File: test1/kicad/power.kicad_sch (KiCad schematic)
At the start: 14 parts, among them J1 1x2 100mil, J2 1x2 100mil, J3 1x2 100mil, U1 TPS7A8401A, U2 TPS22916

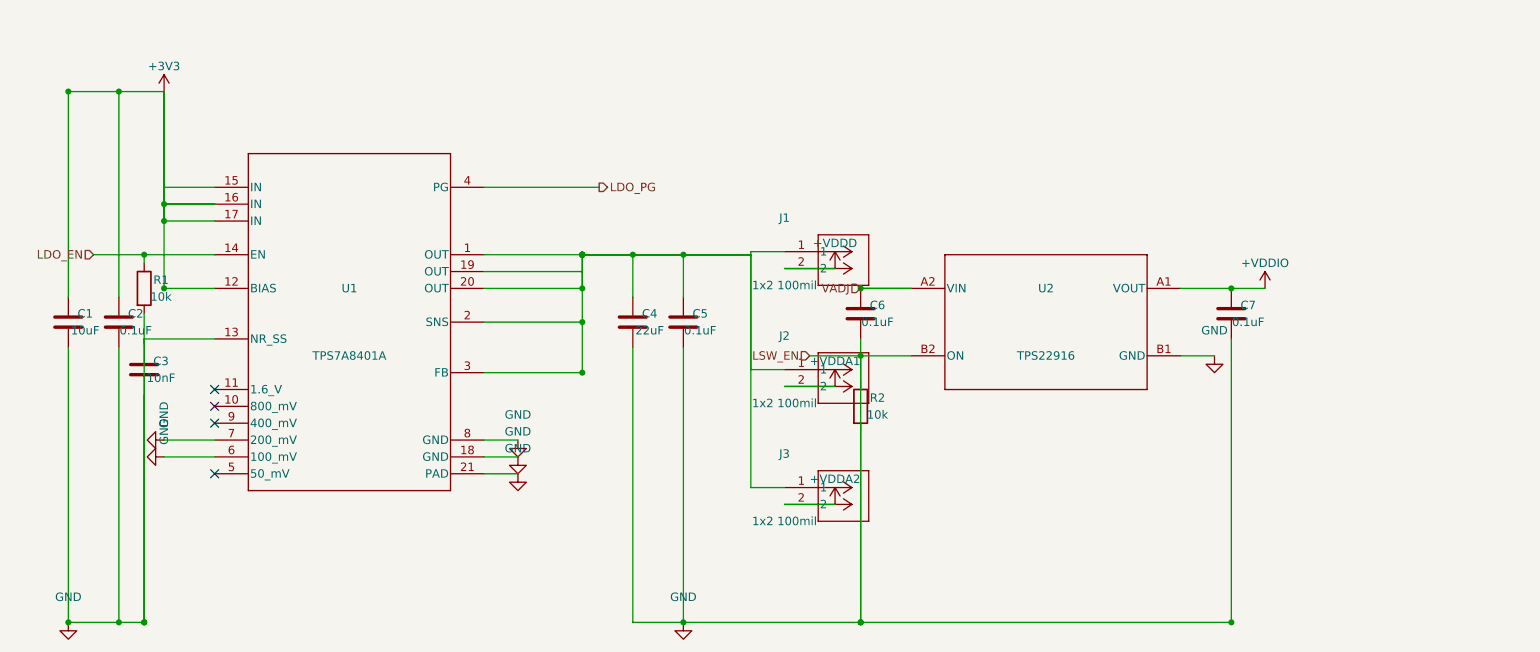
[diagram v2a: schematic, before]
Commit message: Power: separate load-switch cluster from jumper column
The TPS22916 cluster (VADJ label, C6, R2, U2, C7, +VDDIO) was sitting
~4 mm from the jumper column's +VDDx power-symbol labels. R2 and the
LSW_EN hier label collided visually with J2's body.

Fixes:
  - Moved U2 from x=235 → x=270 (35 mm right of jumper power symbols).
  - Reanchored C6, R2, VADJ, and LSW_EN positions to U2 pin coords (no
    hardcoded x), so the whole cluster moves as one if U2 is repositioned
    again.
  - Cleaned up redundant short wire (C6 top → VIN already covered by the
    VADJ→VIN horizontal that passes through C6's pin).

Skill update: cluster separation rule now mentions the label-bounding-box
distance, not just body-to-body — default to ≥25 mm when both adjacent
clusters have side-pointing power symbols or hier labels.

Memory: appended two more lessons to feedback_kicad_generator_lessons.md
(cluster-separation, and "anchor cluster coords to chip pin coords, not
hardcoded constants").

Co-Authored-By: Claude Opus 4.7 (1M context) <noreply@anthropic.com>
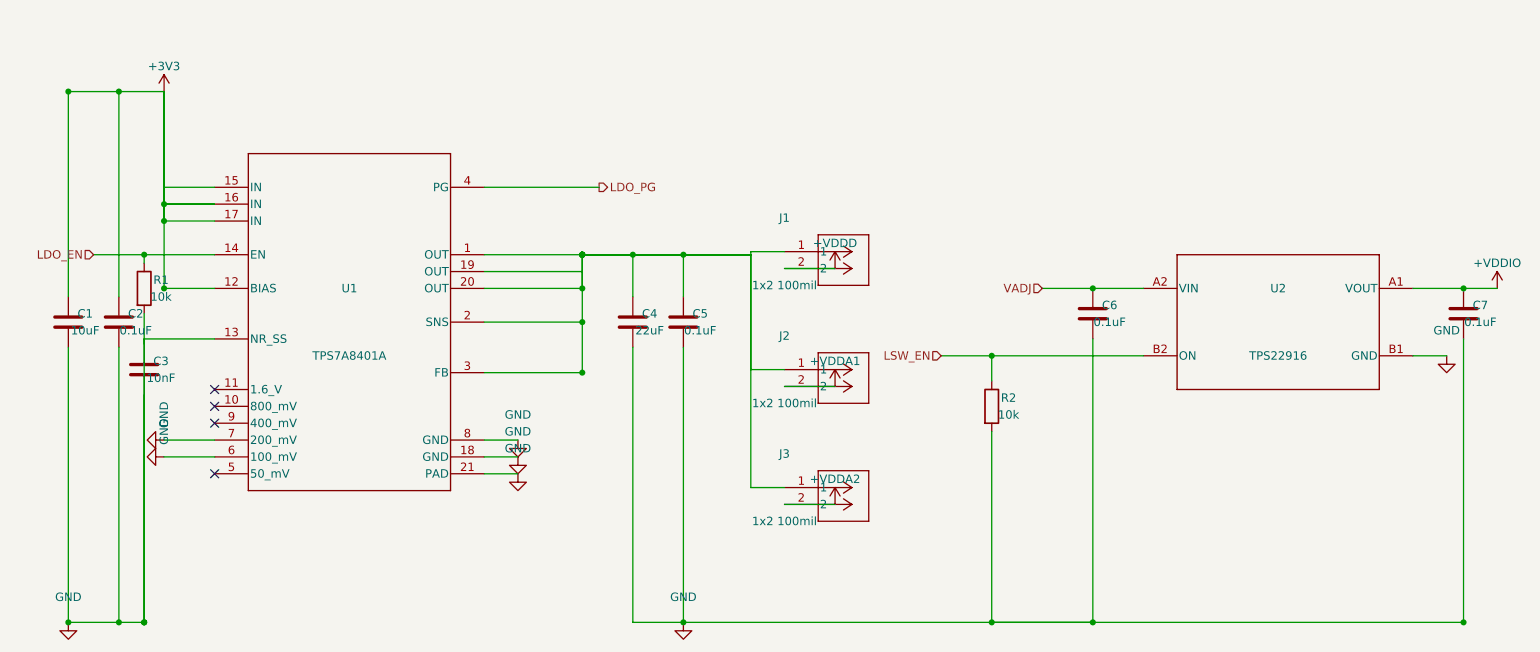
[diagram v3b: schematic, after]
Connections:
- net GND: no longer R2.1, U2.B2 (ON)
- new net LSW_EN: R2.1, U2.B2 (ON)
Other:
- moved on the sheet: C6, C7, R2, U2
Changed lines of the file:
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@@
   (symbol
     (lib_id "Lib:TPS22916CNYFPR")
-    (at 235 130 0)
+    (at 270 130 0)
     (unit 1) (in_bom yes) (on_board yes) (dnp no)
-    (property "Reference" "U2" (at 235 124.92 0) (effects (font (size 1.27 1.27))))
-    (property "Value" "TPS22916" (at 235 135.08 0) (effects (font (size 1.27 1.27))))
+    (property "Reference" "U2" (at 270 124.92 0) (effects (font (size 1.27 1.27))))
+    (property "Value" "TPS22916" (at 270 135.08 0) (effects (font (size 1.27 1.27))))
     (property "Footprint" "Package_DirectFETandLGA:Texas_DSBGA-4_0.6x1.0mm_Layout2x2_P0.4mm" (at 0 0 0) (effects (font (size 1.27 1.27)) (hide yes)))
     (property "Datasheet" "" (at 0 0 0) (effects (font (size 1.27 1.27)) (hide yes)))
@@
       (project "test1"
         (path "/4ed7a046-ef33-57d9-8730-321c05965af3/45af8917-b3aa-56de-8c9b-8d649d910e5f" (reference "U2") (unit 1)))))
-  (wire (pts (xy 214.68 124.92) (xy 207.01 124.92)) (stroke (width 0) (type default)))
-  (hierarchical_label "VADJ" (shape input) (at 207.01 124.92 180) (effects (font (size 1.27 1.27)) (justify right)))
-  (wire (pts (xy 255.32 135.08) (xy 260.4 135.08)) (stroke (width 0) (type default)))
+  (wire (pts (xy 249.68 124.92) (xy 234.44 124.92)) (stroke (width 0) (type default)))
+  (hierarchical_label "VADJ" (shape input) (at 234.44 124.92 180) (effects (font (size 1.27 1.27)) (justify right)))
+  (wire (pts (xy 290.32 135.08) (xy 295.4 135.08)) (stroke (width 0) (type default)))
   (symbol
     (lib_id "power:GND")
-    (at 260.4 135.08 0)
+    (at 295.4 135.08 0)
     (unit 1) (in_bom yes) (on_board yes) (dnp no)
-    (property "Reference" "#PWR151762a4" (at 260.4 128.73000000000002 0) (effects (font (size 1.27 1.27)) (hide yes)))
-    (property "Value" "GND" (at 260.4 131.27 0) (effects (font (size 1.27 1.27))))
+    (property "Reference" "#PWRf65ce50a" (at 295.4 128.73000000000002 0) (effects (font (size 1.27 1.27)) (hide yes)))
+    (property "Value" "GND" (at 295.4 131.27 0) (effects (font (size 1.27 1.27))))
     (property "Footprint" "" (at 0 0 0) (effects (font (size 1.27 1.27)) (hide yes)))
     (property "Datasheet" "" (at 0 0 0) (effects (font (size 1.27 1.27)) (hide yes)))
@@
     (instances
       (project "test1"
-        (path "/4ed7a046-ef33-57d9-8730-321c05965af3/45af8917-b3aa-56de-8c9b-8d649d910e5f" (reference "#PWR151762a4") (unit 1)))))
-  (wire (pts (xy 255.32 124.92) (xy 268.02 124.92)) (stroke (width 0) (type default)))
+        (path "/4ed7a046-ef33-57d9-8730-321c05965af3/45af8917-b3aa-56de-8c9b-8d649d910e5f" (reference "#PWRf65ce50a") (unit 1)))))
+  (wire (pts (xy 290.32 124.92) (xy 303.02 124.92)) (stroke (width 0) (type default)))
   (symbol
     (lib_id "power:+VDDIO")
-    (at 268.02 124.92 0)
+    (at 303.02 124.92 0)
     (unit 1) (in_bom yes) (on_board yes) (dnp no)
-    (property "Reference" "#PWR666eeb67" (at 268.02 118.57000000000001 0) (effects (font (size 1.27 1.27)) (hide yes)))
-    (property "Value" "+VDDIO" (at 268.02 121.11 0) (effects (font (size 1.27 1.27))))
+    (property "Reference" "#PWRd893e26a" (at 303.02 118.57000000000001 0) (effects (font (size 1.27 1.27)) (hide yes)))
+    (property "Value" "+VDDIO" (at 303.02 121.11 0) (effects (font (size 1.27 1.27))))
     (property "Footprint" "" (at 0 0 0) (effects (font (size 1.27 1.27)) (hide yes)))
     (property "Datasheet" "" (at 0 0 0) (effects (font (size 1.27 1.27)) (hide yes)))
@@
     (instances
       (project "test1"
-        (path "/4ed7a046-ef33-57d9-8730-321c05965af3/45af8917-b3aa-56de-8c9b-8d649d910e5f" (reference "#PWR666eeb67") (unit 1)))))
+        (path "/4ed7a046-ef33-57d9-8730-321c05965af3/45af8917-b3aa-56de-8c9b-8d649d910e5f" (reference "#PWRd893e26a") (unit 1)))))
   (symbol
     (lib_id "Device:C")
-    (at 207.06 128.73 0)
+    (at 242.06 128.73 0)
     (unit 1) (in_bom yes) (on_board yes) (dnp no)
-    (property "Reference" "C6" (at 209.6 127.46 0) (effects (font (size 1.27 1.27))))
-    (property "Value" "0.1uF" (at 209.6 130.0 0) (effects (font (size 1.27 1.27))))
+    (property "Reference" "C6" (at 244.6 127.46 0) (effects (font (size 1.27 1.27))))
+    (property "Value" "0.1uF" (at 244.6 130.0 0) (effects (font (size 1.27 1.27))))
     (property "Footprint" "Capacitor_SMD:C_0402_1005Metric" (at 0 0 0) (effects (font (size 1.27 1.27)) (hide yes)))
     (property "Datasheet" "" (at 0 0 0) (effects (font (size 1.27 1.27)) (hide yes)))
@@
       (project "test1"
         (path "/4ed7a046-ef33-57d9-8730-321c05965af3/45af8917-b3aa-56de-8c9b-8d649d910e5f" (reference "C6") (unit 1)))))
-  (wire (pts (xy 207.06 124.92) (xy 214.68 124.92)) (stroke (width 0) (type default)))
-  (junction (at 207.06 124.92) (diameter 0) (color 0 0 0 0))
-  (wire (pts (xy 207.06 132.54) (xy 207.06 175.26)) (stroke (width 0) (type default)))
-  (wire (pts (xy 207.06 175.26) (xy 180.34 175.26)) (stroke (width 0) (type default)))
-  (junction (at 207.06 175.26) (diameter 0) (color 0 0 0 0))
+  (junction (at 242.06 124.92) (diameter 0) (color 0 0 0 0))
+  (wire (pts (xy 242.06 132.54) (xy 242.06 175.26)) (stroke (width 0) (type default)))
+  (wire (pts (xy 242.06 175.26) (xy 180.34 175.26)) (stroke (width 0) (type default)))
+  (junction (at 242.06 175.26) (diameter 0) (color 0 0 0 0))
   (symbol
     (lib_id "Device:C")
-    (at 262.94 128.73 0)
+    (at 297.94 128.73 0)
     (unit 1) (in_bom yes) (on_board yes) (dnp no)
-    (property "Reference" "C7" (at 265.48 127.46 0) (effects (font (size 1.27 1.27))))
-    (property "Value" "0.1uF" (at 265.48 130.0 0) (effects (font (size 1.27 1.27))))
+    (property "Reference" "C7" (at 300.48 127.46 0) (effects (font (size 1.27 1.27))))
+    (property "Value" "0.1uF" (at 300.48 130.0 0) (effects (font (size 1.27 1.27))))
     (property "Footprint" "Capacitor_SMD:C_0402_1005Metric" (at 0 0 0) (effects (font (size 1.27 1.27)) (hide yes)))
     (property "Datasheet" "" (at 0 0 0) (effects (font (size 1.27 1.27)) (hide yes)))
@@
       (project "test1"
         (path "/4ed7a046-ef33-57d9-8730-321c05965af3/45af8917-b3aa-56de-8c9b-8d649d910e5f" (reference "C7") (unit 1)))))
-  (wire (pts (xy 262.94 124.92) (xy 262.94 124.92)) (stroke (width 0) (type default)))
-  (junction (at 262.94 124.92) (diameter 0) (color 0 0 0 0))
-  (wire (pts (xy 262.94 132.54) (xy 262.94 175.26)) (stroke (width 0) (type default)))
-  (wire (pts (xy 207.06 175.26) (xy 262.94 175.26)) (stroke (width 0) (type default)))
-  (junction (at 262.94 175.26) (diameter 0) (color 0 0 0 0))
+  (junction (at 297.94 124.92) (diameter 0) (color 0 0 0 0))
+  (wire (pts (xy 297.94 132.54) (xy 297.94 175.26)) (stroke (width 0) (type default)))
+  (wire (pts (xy 242.06 175.26) (xy 297.94 175.26)) (stroke (width 0) (type default)))
+  (junction (at 297.94 175.26) (diameter 0) (color 0 0 0 0))
   (symbol
     (lib_id "Device:R")
-    (at 207.06 142.70000000000002 0)
+    (at 226.82 142.70000000000002 0)
     (unit 1) (in_bom yes) (on_board yes) (dnp no)
-    (property "Reference" "R2" (at 209.6 141.43 0) (effects (font (size 1.27 1.27))))
-    (property "Value" "10k" (at 209.6 143.97000000000003 0) (effects (font (size 1.27 1.27))))
+    (property "Reference" "R2" (at 229.35999999999999 141.43 0) (effects (font (size 1.27 1.27))))
+    (property "Value" "10k" (at 229.35999999999999 143.97000000000003 0) (effects (font (size 1.27 1.27))))
     (property "Footprint" "Resistor_SMD:R_0402_1005Metric" (at 0 0 0) (effects (font (size 1.27 1.27)) (hide yes)))
     (property "Datasheet" "" (at 0 0 0) (effects (font (size 1.27 1.27)) (hide yes)))
@@
       (project "test1"
         (path "/4ed7a046-ef33-57d9-8730-321c05965af3/45af8917-b3aa-56de-8c9b-8d649d910e5f" (reference "R2") (unit 1)))))
-  (wire (pts (xy 207.06 138.89000000000001) (xy 207.06 135.08)) (stroke (width 0) (type default)))
-  (wire (pts (xy 207.06 135.08) (xy 214.68 135.08)) (stroke (width 0) (type default)))
-  (junction (at 207.06 135.08) (diameter 0) (color 0 0 0 0))
-  (hierarchical_label "LSW_EN" (shape input) (at 199.39 135.08 180) (effects (font (size 1.27 1.27)) (justify right)))
-  (wire (pts (xy 199.39 135.08) (xy 207.06 135.08)) (stroke (width 0) (type default)))
-  (wire (pts (xy 207.06 146.51000000000002) (xy 207.06 175.26)) (stroke (width 0) (type default)))
-  (junction (at 207.06 175.26) (diameter 0) (color 0 0 0 0))
+  (wire (pts (xy 226.82 138.89000000000001) (xy 226.82 135.08)) (stroke (width 0) (type default)))
+  (wire (pts (xy 226.82 135.08) (xy 249.68 135.08)) (stroke (width 0) (type default)))
+  (hierarchical_label "LSW_EN" (shape input) (at 219.20000000000002 135.08 180) (effects (font (size 1.27 1.27)) (justify right)))
+  (wire (pts (xy 219.20000000000002 135.08) (xy 226.82 135.08)) (stroke (width 0) (type default)))
+  (junction (at 226.82 135.08) (diameter 0) (color 0 0 0 0))
+  (wire (pts (xy 226.82 146.51000000000002) (xy 226.82 175.26)) (stroke (width 0) (type default)))
+  (junction (at 226.82 175.26) (diameter 0) (color 0 0 0 0))
+  (wire (pts (xy 242.06 175.26) (xy 226.82 175.26)) (stroke (width 0) (type default)))
   (sheet_instances
     (path "/" (page "3"))

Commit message: Project-wide connectivity audit: refdes uniqueness + hier-label correctness
Added test1/verify_project.py as a kicad-cli-erc substitute (the dev
build doesn't ship _cvpcb.kiface, so sch erc is broken). The verifier
parses all .kicad_sch files and checks:
  1. Duplicate refdes (KiCad's refdes namespace is project-wide).
  2. Parent sheet-pin name + direction matches child hierarchical_label.
  3. Orphan child hierarchical_labels (no matching parent pin).

First run flagged 48 issues. Now reports 0.

Refdes scheme — per-sheet decade ranges so global namespace stays unique:
  FMC 1-9 (J1-J4)
  Power 10-19 (U10/U11, R10/R11, C10-C16, J10-J12)
  Bobcat 20-29 (U20, R20/R21, C20-C25)
  EEPROM 30-39 (U30, R30/R31, C30)
  Bias 40-49 (U40/U41 [U41 dual-unit OPA], Q40-Q43, R40/R41, C40-C43)
  Connectors 50-59 (J50-J57, TP50-TP52)

Hierarchical / global label rework:
  - Parent sheet-pin directions corrected to match child labels (was
    flipped on every Bobcat SPI pin and on FMC's LDO_EN/LSW_EN/LDO_PG).
  - Bobcat SPI labels: passive → input/output as appropriate.
  - Project-wide nets converted to global_label (auto-tie by name, no
    parent pins): SCL, SDA, SAMPLE_OUT*, OSC_EN, WEIGHT_EN, SAMPLE_TRIG,
    BIAS_ISO0/1, CS_L, SCLK, MOSI, MISO, SPI_DMODE, RESET_N.
  - hier_label retained for clean 2-sheet pairs: VADJ, LDO_EN, LDO_PG,
    LSW_EN (FMC ↔ Power); BIAS0/1 (Bias ↔ Bobcat); CLK_OUT0-3, GPIO0-3
    (Bobcat ↔ Connectors).
  - Visual cue in renders: globals render as boxed rectangles; hierarchical
    labels render as arrows — handy when scanning a sheet.

Memory: appended five connectivity-correctness lessons to
feedback_kicad_generator_lessons.md (refdes namespace, parent/child
direction parity, no-passive-for-real-signals, global vs hier decision
table, verify-after-every-change).

Co-Authored-By: Claude Opus 4.7 (1M context) <noreply@anthropic.com>
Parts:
- removed C1: 10uF, Capacitor_SMD:C_0805_2012Metric, symbol Device:C
- removed C2, C5, C6, C7: 0.1uF, Capacitor_SMD:C_0402_1005Metric, symbol Device:C
- removed C3: 10nF, Capacitor_SMD:C_0402_1005Metric, symbol Device:C
- removed C4: 22uF, Capacitor_SMD:C_0805_2012Metric, symbol Device:C
- removed J1, J2, J3: 1x2 100mil, Connector_PinHeader_2.54mm:PinHeader_1x02_P2.54mm_Vertical, symbol Lib:TSW-102-05-G-S
- removed R1, R2: 10k, Resistor_SMD:R_0402_1005Metric, symbol Device:R
- removed U1: TPS7A8401A, Package_DFN_QFN:VQFN-20-1EP_3.5x3.5mm_P0.5mm_EP1.6x1.6mm, symbol Lib:TPS7A8401A
- removed U2: TPS22916, Package_DirectFETandLGA:Texas_DSBGA-4_0.6x1.0mm_Layout2x2_P0.4mm, symbol Lib:TPS22916CNYFPR
- added C10: 10uF, Capacitor_SMD:C_0805_2012Metric, symbol Device:C
- added C11, C14, C15, C16: 0.1uF, Capacitor_SMD:C_0402_1005Metric, symbol Device:C
- added C12: 10nF, Capacitor_SMD:C_0402_1005Metric, symbol Device:C
- added C13: 22uF, Capacitor_SMD:C_0805_2012Metric, symbol Device:C
- added J10, J11, J12: 1x2 100mil, Connector_PinHeader_2.54mm:PinHeader_1x02_P2.54mm_Vertical, symbol Lib:TSW-102-05-G-S
- added R10, R11: 10k, Resistor_SMD:R_0402_1005Metric, symbol Device:R
- added U10: TPS7A8401A, Package_DFN_QFN:VQFN-20-1EP_3.5x3.5mm_P0.5mm_EP1.6x1.6mm, symbol Lib:TPS7A8401A
- added U11: TPS22916, Package_DirectFETandLGA:Texas_DSBGA-4_0.6x1.0mm_Layout2x2_P0.4mm, symbol Lib:TPS22916CNYFPR
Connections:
- net +3V3: now also C10.1, C11.1, U10.12 (BIAS), U10.15 (IN), U10.16 (IN), U10.17 (IN)
- net +VDDA1: now also J11.2
- net +VDDA2: now also J12.2
- net +VDDD: now also J10.2
- net +VDDIO: now also C16.1, U11.A1 (VOUT)
- net GND: now also C10.2, C11.2, C12.1, C12.2, C13.2, C14.2, C15.2, C16.2, R10.2, R11.2, U10.13 (NR_SS), U10.18 (GND), U10.21 (PAD), U10.6 (100_mV), U10.7 (200_mV), U10.8 (GND), U11.B1 (GND)
- net LDO_EN: now also R10.1, U10.14 (EN)
- net LDO_PG: now also U10.4 (PG)
- net LSW_EN: now also R11.1, U11.B2 (ON)
- net VADJ: now also C15.1, U11.A2 (VIN)
- new net: C13.1, C14.1, J10.1, J11.1, J12.1, U10.1 (OUT), U10.2 (SNS), U10.20 (OUT), U10.3 (FB)

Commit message: Split test1 generator into per-sheet package with netlist YAML + strict validator
Combines three layered changes:

1. Apply the design-review audit (test1/error_log.md): 9 ERRORs + 10
   WARNINGs from the new .claude/skills/design_review.md skill — FMC
   LA-bank 0Ω routing, Bobcat SPI/control/GPIO pull network, LDO
   ANY-OUT to FPGA, LDO_PG pull-up + series, bias DNP convention,
   kelvin SNS, per-pin VDDIO + bulk caps, BIAS bypass, VADJ/VDDIO bulk,
   MCP4728 EEPROM provisioning notes, shared-rail decision documented.

2. Refactor test1/gen_schematic.py (1825 lines → 138-line entry point)
   into a per-sheet package at test1/gen/:
     config.py / symbols.py / shared.py  — primitives, Sheet container,
     LA_ASSIGN, footprints, sexpr emit
     build_<sheet>.py × 7                — one builder per child sheet
     netlist.py / validator.py           — YAML loader + strict checker
   Per-session context for any single sheet drops to ~500 lines.
   Also sorts non-deterministic set iteration that made fmc.kicad_sch
   diff noisily across runs.

3. Add a declarative connectivity layer (netlist/<sheet>.yaml):
   parts inventory + nets (power / hier / global / internal), with
   explicit unit syntax for multi-unit symbols (U41:u2.7, J3:u3.G16).
   The strict validator runs at the end of every build_<sheet>() call:
     - inventory: YAML parts ↔ placed (refdes, unit) parity
     - connectivity: every YAML net member is in a connected component
       named the YAML net name (Union-Find on wires + junctions + label
       anchors + power-symbol pins; T-intersections auto-connect)
     - internal nets: members in one component, no name check
   Sheet now records structured PlacedPart/wire/label data alongside
   the s-expr emit; validator reads those instead of re-parsing.

All 6 child sheets' .kicad_sch outputs are byte-identical to the
post-design-review reference, and verify_project.py reports 0 issues.

Co-Authored-By: Claude Opus 4.7 (1M context) <noreply@anthropic.c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
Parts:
- added C17: 1uF, Capacitor_SMD:C_0402_1005Metric, symbol Device:C
- added R12: 10k, Resistor_SMD:R_0402_1005Metric, symbol Device:R
- added R13: 1k, Resistor_SMD:R_0402_1005Metric, symbol Device:R
- C15, C16: value 0.1uF -> 1uF
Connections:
- net +3V3: now also C17.1, R12.1
- net GND: now also C17.2; no longer U10.6 (100_mV), U10.7 (200_mV)
- net LDO_PG: now also R13.2; no longer U10.4 (PG)
- net LDO_SET_800mV: now reaches U10.10 (800_mV)
- net LDO_SET_1V6: now reaches U10.11 (1.6_V)
- net LDO_SET_50mV: now reaches U10.5 (50_mV)
- net LDO_SET_400mV: now reaches U10.9 (400_mV)
- new net: R12.2, R13.1, U10.4 (PG)
- new net LDO_SET_100mV: U10.6 (100_mV)
- new net LDO_SET_200mV: U10.7 (200_mV)
- no-connect marks 4 -> 0
